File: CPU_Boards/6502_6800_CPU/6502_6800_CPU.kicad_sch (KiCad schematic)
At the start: 63 parts, among them J10 Conn_01x12, J13 GAL_20x10, J14 Conn_01x12, J15 Conn_01x12, J16 Conn_01x12, J17 GAL_20x10, J18 Conn_01x09, J19 Conn_01x08, J20 Conn_01x08, J21 Conn_01x09, J22 JTAG, J23 Conn_01x12, J29 Conn_01x12, J30 Conn_02x02_Odd_Even, J31 Conn_02x02_Odd_Even, J35 GAL_20x10, J5 Conn_01x01, J6 Spare, J7 Outside, J8 Conn_01x01, J9 Conn_01x01, U7 W65C02SxP, U8 MC6802, U9 XC9572VQ44

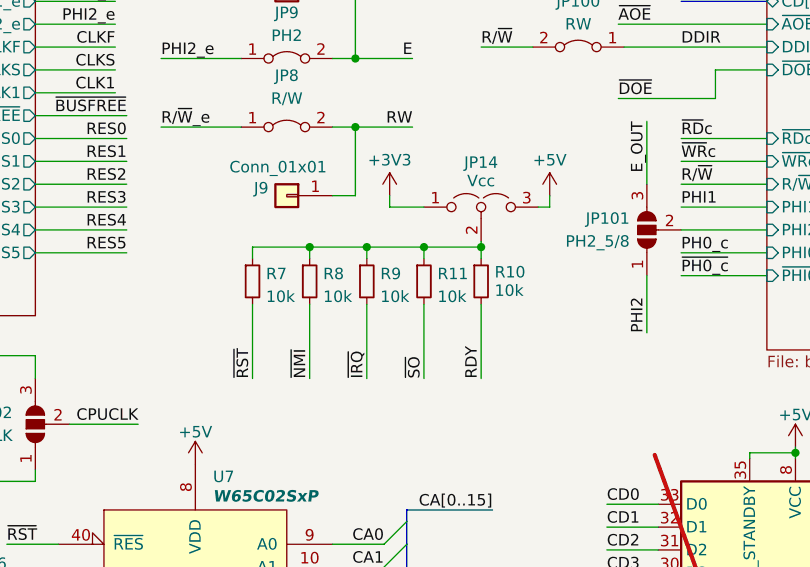
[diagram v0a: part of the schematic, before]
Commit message: first boards manufactured
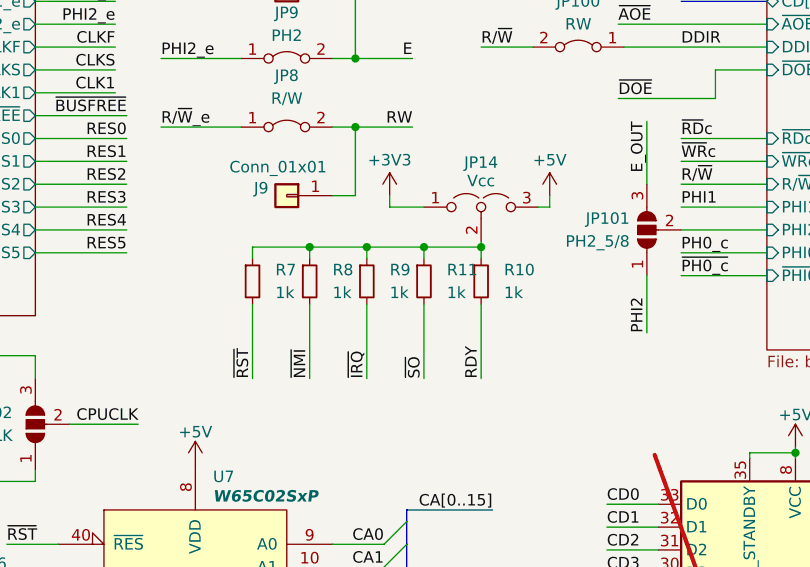
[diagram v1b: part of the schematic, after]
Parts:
- J10, J13, J14, J15, J16, J17, J18, J19, J20, J21, J23, J29, J30, J31, J35, J5, J6, J8, J9, JP1, JP10, JP100, JP101, JP102, JP11, JP12, JP13, JP14, JP15, JP2, JP3, JP4, JP5, JP6, JP7, JP8, JP9: now left out of the parts list
- R10, R11, R7, R8, R9: value 10k -> 1k
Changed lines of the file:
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@@
 		(unit 1)
 		(exclude_from_sim no)
-		(in_bom yes)
+		(in_bom no)
 		(on_board yes)
 		(dnp no)
@@
 		(unit 1)
 		(exclude_from_sim no)
-		(in_bom yes)
+		(in_bom no)
 		(on_board yes)
 		(dnp no)
@@
 		(unit 1)
 		(exclude_from_sim yes)
-		(in_bom yes)
+		(in_bom no)
 		(on_board yes)
 		(dnp no)
@@
 		(fields_autoplaced yes)
 		(property "Reference" "R7"
-			(at 75.1586 54.4103 0)
+			(at 76.2 53.9749 0)
 			(effects
 				(font
@@
 			)
 		)
-		(property "Value" "10k"
-			(at 75.1586 56.9472 0)
+		(property "Value" "1k"
+			(at 76.2 56.5149 0)
 			(effects
 				(font
@@
 		(unit 1)
 		(exclude_from_sim no)
-		(in_bom yes)
+		(in_bom no)
 		(on_board yes)
 		(dnp no)
@@
 		(unit 1)
 		(exclude_from_sim no)
-		(in_bom yes)
+		(in_bom no)
 		(on_board yes)
 		(dnp no)
@@
 		(unit 1)
 		(exclude_from_sim no)
-		(in_bom yes)
+		(in_bom no)
 		(on_board yes)
 		(dnp no)
@@
 		(unit 1)
 		(exclude_from_sim no)
-		(in_bom yes)
+		(in_bom no)
 		(on_board yes)
 		(dnp no)
@@
 		(unit 1)
 		(exclude_from_sim yes)
-		(in_bom yes)
+		(in_bom no)
 		(on_board yes)
 		(dnp no)
@@
 		(unit 1)
 		(exclude_from_sim no)
-		(in_bom yes)
+		(in_bom no)
 		(on_board yes)
 		(dnp no)
@@
 		(unit 1)
 		(exclude_from_sim no)
-		(in_bom yes)
+		(in_bom no)
 		(on_board yes)
 		(dnp no)
@@
 		(fields_autoplaced yes)
 		(property "Reference" "R8"
-			(at 81.5086 54.4103 0)
+			(at 82.55 53.9749 0)
 			(effects
 				(font
@@
 			)
 		)
-		(property "Value" "10k"
-			(at 81.5086 56.9472 0)
+		(property "Value" "1k"
+			(at 82.55 56.5149 0)
 			(effects
 				(font
@@
 		(unit 1)
 		(exclude_from_sim no)
-		(in_bom yes)
+		(in_bom no)
 		(on_board yes)
 		(dnp no)
@@
 		(unit 1)
 		(exclude_from_sim no)
-		(in_bom yes)
+		(in_bom no)
 		(on_board yes)
 		(dnp no)
@@
 		(unit 1)
 		(exclude_from_sim no)
-		(in_bom yes)
+		(in_bom no)
 		(on_board yes)
 		(dnp no)
@@
 		(unit 1)
 		(exclude_from_sim no)
-		(in_bom yes)
+		(in_bom no)
 		(on_board yes)
 		(dnp no)
@@
 		(fields_autoplaced yes)
 		(property "Reference" "R11"
-			(at 94.2086 54.4103 0)
+			(at 95.25 53.9749 0)
 			(effects
 				(font
@@
 			)
 		)
-		(property "Value" "10k"
-			(at 94.2086 56.9472 0)
+		(property "Value" "1k"
+			(at 95.25 56.5149 0)
 			(effects
 				(font
@@
 		(unit 1)
 		(exclude_from_sim no)
-		(in_bom yes)
+		(in_bom no)
 		(on_board yes)
 		(dnp no)
@@
 		(unit 1)
 		(exclude_from_sim no)
-		(in_bom yes)
+		(in_bom no)
 		(on_board yes)
 		(dnp no)
@@
 		(unit 1)
 		(exclude_from_sim no)
-		(in_bom yes)
+		(in_bom no)
 		(on_board yes)
 		(dnp no)
@@
 		(unit 1)
 		(exclude_from_sim no)
-		(in_bom yes)
+		(in_bom no)
 		(on_board yes)
 		(dnp no)
@@
 		(unit 1)
 		(exclude_from_sim no)
-		(in_bom yes)
+		(in_bom no)
 		(on_board yes)
 		(dnp no)
@@
 		(unit 1)
 		(exclude_from_sim yes)
-		(in_bom yes)
+		(in_bom no)
 		(on_board yes)
 		(dnp no)
@@
 		(unit 1)
 		(exclude_from_sim no)
-		(in_bom yes)
+		(in_bom no)
 		(on_board yes)
 		(dnp no)
@@
 		(unit 1)
 		(exclude_from_sim no)
-		(in_bom yes)
+		(in_bom no)
 		(on_board yes)
 		(dnp no)
@@
 		(unit 1)
 		(exclude_from_sim no)
-		(in_bom yes)
+		(in_bom no)
 		(on_board yes)
 		(dnp no)
@@
 		(unit 1)
 		(exclude_from_sim no)
-		(in_bom yes)
+		(in_bom no)
 		(on_board yes)
 		(dnp no)
@@
 		(unit 1)
 		(exclude_from_sim yes)
-		(in_bom yes)
+		(in_bom no)
 		(on_board yes)
 		(dnp no)
@@
 		(unit 1)
 		(exclude_from_sim no)
-		(in_bom yes)
+		(in_bom no)
 		(on_board yes)
 		(dnp no)
@@
 		(unit 1)
 		(exclude_from_sim yes)
-		(in_bom yes)
+		(in_bom no)
 		(on_board yes)
 		(dnp no)
@@
 		(unit 1)
 		(exclude_from_sim no)
-		(in_bom yes)
+		(in_bom no)
 		(on_board yes)
 		(dnp no)
@@
 		(unit 1)
 		(exclude_from_sim yes)
-		(in_bom yes)
+		(in_bom no)
 		(on_board yes)
 		(dnp no)
@@
 		(unit 1)
 		(exclude_from_sim no)
-		(in_bom yes)
+		(in_bom no)
 		(on_board yes)
 		(dnp no)
@@
 		(unit 1)
 		(exclude_from_sim no)
-		(in_bom yes)
+		(in_bom no)
 		(on_board yes)
 		(dnp no)
@@
 		(unit 1)
 		(exclude_from_sim no)
-		(in_bom yes)
+		(in_bom no)
 		(on_board yes)
 		(dnp no)
@@
 		(unit 1)
 		(exclude_from_sim no)
-		(in_bom yes)
+		(in_bom no)
 		(on_board yes)
 		(dnp no)
@@
 		(fields_autoplaced yes)
 		(property "Reference" "R9"
-			(at 87.8586 54.4103 0)
+			(at 88.9 53.9749 0)
 			(effects
 				(font
@@
 			)
 		)
-		(property "Value" "10k"
-			(at 87.8586 56.9472 0)
+		(property "Value" "1k"
+			(at 88.9 56.5149 0)
 			(effects
 				(font
@@
 		(unit 1)
 		(exclude_from_sim no)
-		(in_bom yes)
+		(in_bom no)
 		(on_board yes)
 		(dnp no)
@@
 		(unit 1)
 		(exclude_from_sim no)
-		(in_bom yes)
+		(in_bom no)
 		(on_board yes)
 		(dnp no)
@@
 		(unit 1)
 		(exclude_from_sim no)
-		(in_bom yes)
+		(in_bom no)
 		(on_board yes)
 		(dnp no)
@@
 		(fields_autoplaced yes)
 		(property "Reference" "R10"
-			(at 100.5586 54.221 0)
+			(at 101.6 53.9749 0)
 			(effects
 				(font
@@
 			)
 		)
-		(property "Value" "10k"
-			(at 100.5586 56.269 0)
+		(property "Value" "1k"
+			(at 101.6 56.5149 0)
 			(effects
 				(font
@@
 		(unit 1)
 		(exclude_from_sim no)
-		(in_bom yes)
+		(in_bom no)
 		(on_board yes)
 		(dnp no)
